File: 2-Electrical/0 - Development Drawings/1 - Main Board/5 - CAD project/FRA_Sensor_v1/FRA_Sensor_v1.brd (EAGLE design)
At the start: 79 x 94 mm, 141 parts, among them IC1 CP2101, IC2 LMV611, IC3 TS520533, J2 ETH_CONN, J3 USB, Q1 Si2300DS, Q2 FDN306P, T1 BC847, T2 BC847, T3 BC847, U2 ESP-WROOM-32, Y3 32.768kHz

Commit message: sch
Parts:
- removed C21, C22: 10u, resistor:C0603K
- removed C23: 220u, resistor:153CLV-0605
- removed C31: 100n, resistor:C0603K
- removed C8: DNI, resistor:C0603K
- removed L1: 2.2uH, resistor:L3225M
- removed LIGHT_DR: LDR, pinhead:1X02
- removed R20: 1G, resistor:R0603
- removed R26: 0, resistor:R0603
- removed R27: DNI, resistor:R0603
- removed R41, R45, R46: 12k, resistor:R0603
- removed TP13, TP28, TP29, TP30: TPTP10R, testpad:TP10R
- added D4, D6: PESD1CAN, diode:SOT23
- added D7, D8: (no value), SparkFun-LED:LED_5MM
- added J1: (no value), con-jack:SPC4078
- added LIGHT_DR1: LDR, pinhead:1X02
- added R68, R69: 10K, resistor:R0603
- added S1, S2: (no value), adafruit:B3F-31XX
- added TP1, TP2, TP3, TP4: TPTP10R, testpad:TP10R
- added U$5, U$6: MOUNTINGHOLE3.0THIN, microbuilder:MOUNTINGHOLE_3.0_PLATEDTHIN
- added X1: TB001-500-02BE, con-wago-500:W237-102
- C10, C17: value 10u -> DNI
- C29, C30: value 22p(DNI) -> 22p
- C7: value DNI -> 220u; device resistor:C0603K -> resistor:153CLV-0605
- R14: value 220k -> 100
- R15: value 100k -> 100
- R18: value 2M7 -> 100
- R19: value 47k -> 100
- R53, R54: value 10k -> 100k
- moved R14 611.4 mm to (-141.0, -533.4), turned to 0 degrees
- moved R15 601.1 mm to (-141.0, -538.5), flipped to the top, turned to 0 degrees
- moved R19 576.8 mm to (-141.0, -548.6), turned to 0 degrees
- moved R18 567.6 mm to (-141.0, -543.6), turned to 0 degrees
- moved C7 244.8 mm to (-119.4, -486.4)
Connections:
- net N$12 renamed P_RTC
- net N$13 renamed N_RTC
- removed net ADC: C31.2, R14.2, R15.2
- removed net N$14: LIGHT_DR.2, R14.1, R18.1, R19.2, R20.1
- removed net N$16: D3.1
- removed net N$27: R41.1
- removed net N$37: L1.1
- removed net N$40: R45.2, R46.1
- removed net N$9: C7.1, C8.2, R26.2, R27.1
- new net BTN1: R68.1, S1.1, U2.24
- new net BTN2: R69.1, S2.1, U2.26
- new net LED: R18.2, R19.2, U2.27
- new net N$6: D8.A, R18.1, R19.1
- new net N$7: D7.A, R14.1, R15.1
- net 3.3V: now also D6.3, R14.2, R15.2, R68.2, R69.2, TP2.TP; no longer C21.1, C23.+, C8.1, L1.2, LIGHT_DR.1, R18.2, R20.2, R26.1, R46.2, TP11.TP
- net 5V: now also TP3.TP; no longer C22.1, R41.2, TP28.TP, TP29.TP
- net GND: now also C7.-, D4.1, D4.2, D6.1, D6.2, D7.K, D8.K, J1.1, J1.2, S1.2, S2.2, X1.2; no longer C21.2, C22.2, C23.-, C31.1, C7.2, R15.1, R19.1, R27.2, R45.1, TP13.TP, TP30.TP
- net N$22: now also TP4.TP
- net N$23: now also TP1.TP
- net N$35: no longer C20.2
- net NRST: now also JTAG1.10, U$2.1
- net RXD0: now also U$2.5
- net TXD0: now also U$2.3
- net VIN: now also D4.3, J1.3, X1.1
- net VIN_PROTECTED: now also C7.+, TP11.TP
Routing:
- net GND: track 469.8 -> 80.2 mm, vias 29 -> 10
- net 3.3V: track 306.9 -> 29.1 mm, vias 26 -> 17
- net 5V: track 183.5 -> 5.38 mm, vias 9 -> 0
- net PWM: track 118.3 -> 0.00 mm, vias 3 -> 0
- net N$14: track 117.3 -> 0.00 mm, vias 2 -> 0
- net ADC: track 70.3 -> 0.00 mm, vias 5 -> 0
- net N$40: track 22.6 -> 0.00 mm, vias 2 -> 0
- net N$27: track 18.0 -> 0.00 mm, vias 2 -> 0
- net N$16: track 5.14 -> 0.00 mm
- net P_RTC: track 6.97 -> 2.57 mm
- net N_RTC: track 7.27 -> 3.60 mm
- net N$35: track 4.44 -> 2.12 mm
- net N$37: track 0.64 -> 0.00 mm
- removed copper zone on layer 1, net 5V
- removed copper zone on layer 16, net 5V
- removed copper zone on layer 16, net VBAT
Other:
- board text added: "06/2019"
- board text added: "FRA Sensor Unit Main PCB"
- board text removed: "12/2018"
- board text removed: "Alarm Light v2"
- board text removed: "X"
- board text removed: "Y"
- board text removed: "Z"

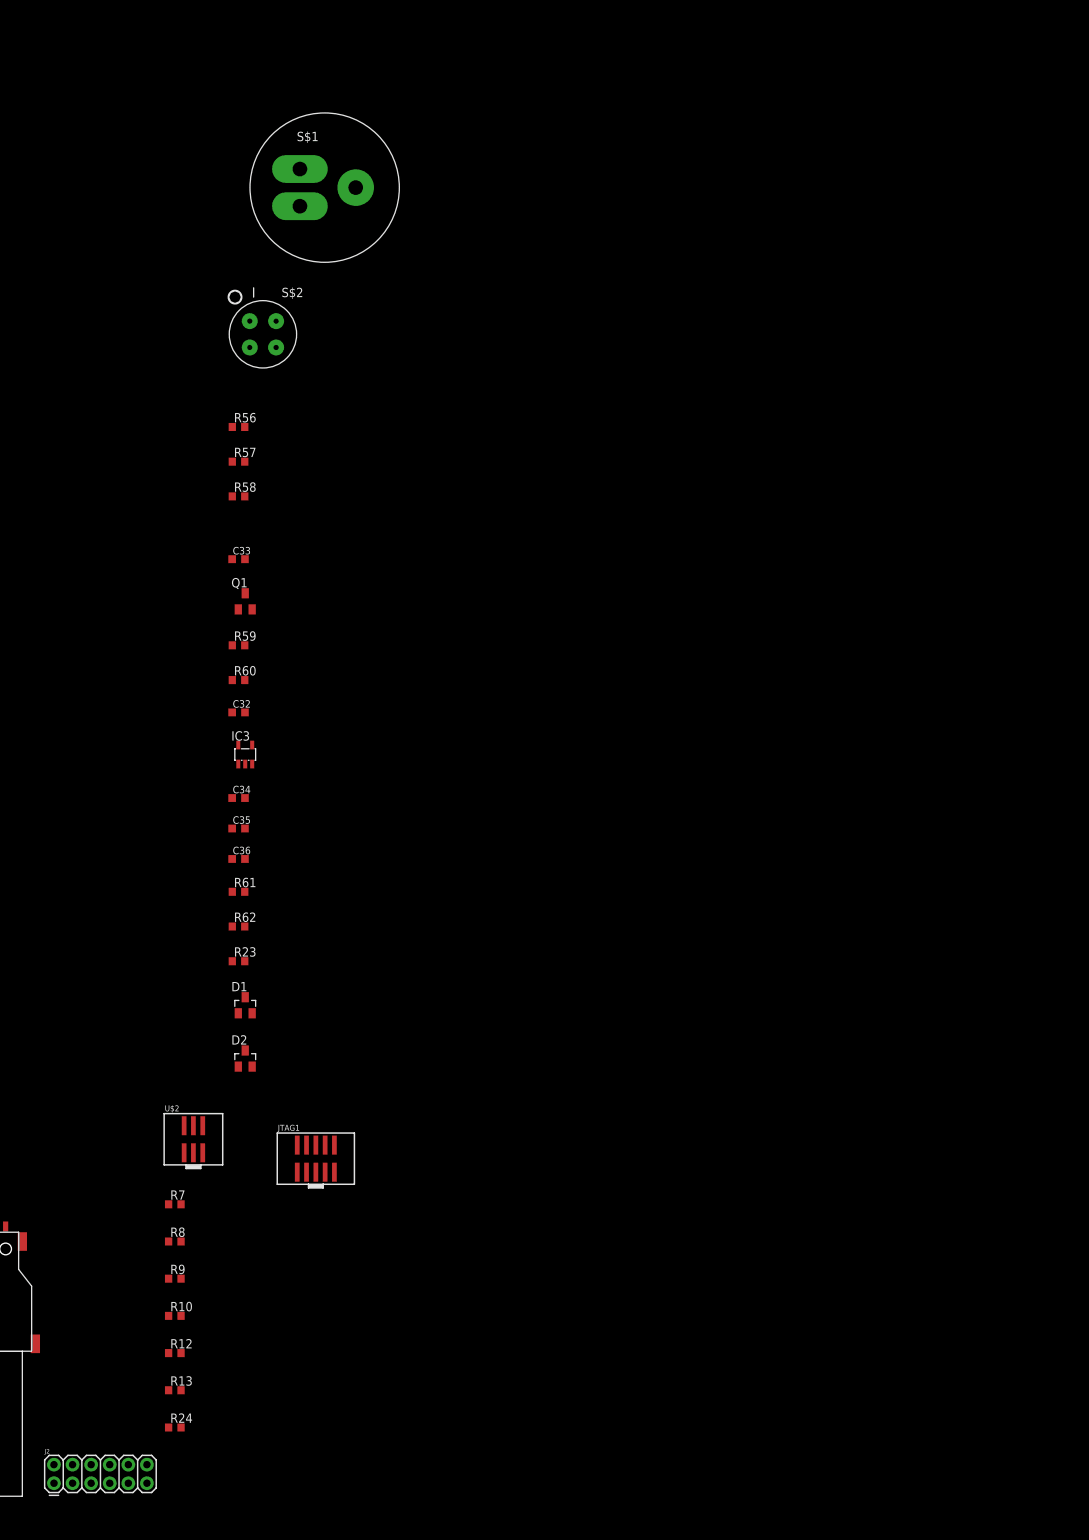
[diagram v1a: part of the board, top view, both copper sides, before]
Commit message: dev and sd
mac address changed
other sample testing
sd card example setup
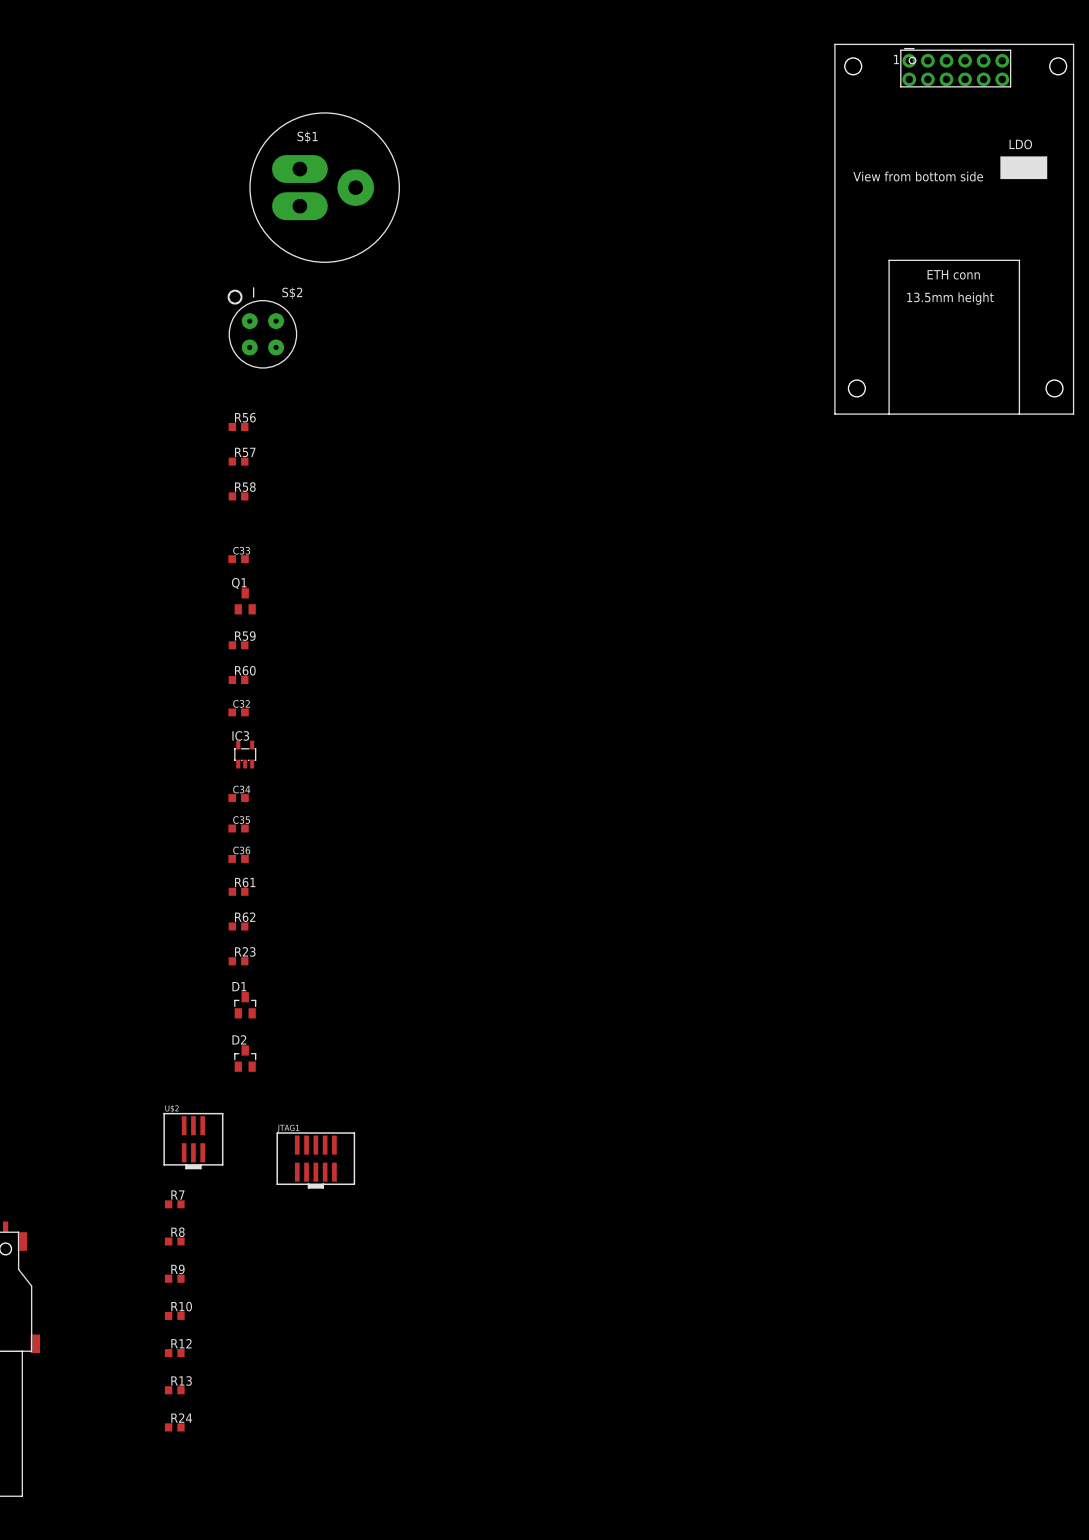
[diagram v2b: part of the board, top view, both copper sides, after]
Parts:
- added U$7: ETH_MODULE_OUTLINE, FRA_eagle_lib:ETH_MODULE_OUTLINE
- moved J2 226.7 mm to (73.7, -30.5), flipped to the bottom, turned to 180 degrees
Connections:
- new net ETH_5V: J2.12
- new net ETH_CLKOUT: J2.9
- new net ETH_INT: J2.10
- new net ETH_RST: J2.4
- new net ETH_WOL: J2.7
- net 3.3V: now also C39.1, C40.1, J2.2
- net BTN1: no longer U2.24
- net BTN2: no longer U2.26
- net GND: now also J2.1, J2.11
- net SD_CS_MCU: now also U2.28; no longer U2.10
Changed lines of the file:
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@@
 <element name="R24" library="resistor" package="R0603" value="100" x="-26.67" y="-217.17"/>
 <element name="U$3" library="adafruit" package="MICROSD" value="MICROSD" x="-67.31" y="-191.77"/>
-<element name="J2" library="SparkFun-Connectors" package="2X6" value="ETH_CONN" x="-43.18" y="-224.79">
-<attribute name="PROD_ID" value="CONN-12423" x="-43.18" y="-224.79" size="1.778" layer="27" display="off"/>
+<element name="J2" library="SparkFun-Connectors" package="2X6" value="ETH_CONN" x="73.66" y="-30.48" rot="MR180">
+<attribute name="PROD_ID" value="CONN-12423" x="73.66" y="-30.48" size="1.778" layer="28" rot="MR180" display="off"/>
 </element>
 <element name="J4" library="sd-mmc" package="SDCMF-10915W010" value="" x="-59.69" y="-203.2"/>
@@
 <element name="R18" library="resistor" package="R0603" value="100" x="-140.97" y="-543.56"/>
 <element name="R19" library="resistor" package="R0603" value="100" x="-140.97" y="-548.64"/>
+<element name="U$7" library="FRA_eagle_lib" package="ETH_MODULE_OUTLINE" value="ETH_MODULE_OUTLINE" x="63.5" y="-78.74"/>
 </elements>
 <signals>
@@
 <contactref element="S2" pad="2"/>
 <contactref element="S1" pad="2"/>
+<contactref element="J2" pad="1"/>
+<contactref element="J2" pad="11"/>
 <wire x1="-53.71" y1="-206.21" x2="-45.72" y2="-205.74" width="0" layer="19" extent="1-1"/>
 <wire x1="-63.81" y1="-202.81" x2="-53.71" y2="-206.21" width="0" layer="19" extent="1-1"/>
@@
 <wire x1="-72.898" y1="-191.77" x2="-65.024" y2="-189.738" width="0" layer="19" extent="1-1"/>
 <wire x1="-47.498" y1="-191.77" x2="-57.404" y2="-189.738" width="0" layer="19" extent="1-1"/>
+<wire x1="73.66" y1="-30.48" x2="-45.72" y2="-205.74" width="0" layer="19" extent="1-1"/>
+<wire x1="86.36" y1="-30.48" x2="73.66" y2="-30.48" width="0" layer="19" extent="1-1"/>
 <wire x1="-25.82" y1="-196.85" x2="-45.72" y2="-205.74" width="0" layer="19" extent="1-1"/>
 <wire x1="-24.13" y1="-175.95" x2="-25.82" y2="-196.85" width="0" layer="19" extent="1-1"/>
@@
 <wire x1="-18.816465625" y1="-89.983859375" x2="-17.088265625" y2="-98.564190625" width="0" layer="19" extent="1-1"/>
 <wire x1="-17.116465625" y1="-80.501196875" x2="-18.816465625" y2="-89.983859375" width="0" layer="19" extent="1-1"/>
-<wire x1="-72.07" y1="-257.84" x2="-72.898" y2="-205.74" width="0" layer="19" extent="1-1"/>
+<wire x1="-72.07" y1="-257.84" x2="73.66" y2="-30.48" width="0" layer="19" extent="1-1"/>
 <wire x1="-70.245" y1="-276.86" x2="-72.07" y2="-257.84" width="0" layer="19" extent="1-1"/>
 <wire x1="-70.245" y1="-281.94" x2="-70.245" y2="-276.86" width="0" layer="19" extent="1-1"/>
@@
 <wire x1="40.768428125" y1="4.974340625" x2="-17.116465625" y2="-80.501196875" width="0" layer="19" extent="1-1"/>
 <wire x1="44.7675" y1="3.595" x2="40.768428125" y2="4.974340625" width="0" layer="19" extent="1-1"/>
+<wire x1="48.9975" y1="3.4925" x2="44.7675" y2="3.595" width="0" layer="19" extent="1-1"/>
+<wire x1="56.4125" y1="6.985" x2="48.9975" y2="3.4925" width="0" layer="19" extent="1-1"/>
+<wire x1="52.3875" y1="11.43" x2="56.4125" y2="6.985" width="0" layer="19" extent="1-1"/>
+<wire x1="41.91" y1="25.64" x2="47.3075" y2="13.97" width="0" layer="19" extent="1-16"/>
+<wire x1="27.94" y1="34.29" x2="34.925" y2="25.64" width="0" layer="19" extent="16-16"/>
+<wire x1="29.5275" y1="36.195" x2="27.94" y2="34.29" width="0" layer="19" extent="1-1"/>
+<wire x1="13.6525" y1="34.5025" x2="27.94" y2="34.29" width="0" layer="19" extent="16-16"/>
+<wire x1="5.715" y1="54.37" x2="5.715" y2="54.2925" width="0" layer="19" extent="16-16"/>
+<wire x1="66.1175" y1="21.9075" x2="52.3875" y2="11.43" width="0" layer="19" extent="1-16"/>
+<wire x1="75.2475" y1="13.0175" x2="66.1175" y2="21.9075" width="0" layer="19" extent="16-16"/>
+<wire x1="69.5325" y1="46.355" x2="66.1175" y2="24.13" width="0" layer="19" extent="16-16"/>
+<wire x1="69.5325" y1="49.2125" x2="69.5325" y2="46.355" width="0" layer="19" extent="1-1"/>
+<wire x1="63.1825" y1="50.165" x2="69.5325" y2="49.2125" width="0" layer="19" extent="1-1"/>
+<wire x1="54.9275" y1="45.4025" x2="63.1825" y2="50.165" width="0" layer="19" extent="1-1"/>
+<wire x1="52.07" y1="55.245" x2="54.9275" y2="45.4025" width="0" layer="19" extent="1-1"/>
+<wire x1="77.2" y1="58.31" x2="69.5325" y2="49.2125" width="0" layer="19" extent="1-1"/>
+<wire x1="69.5" y1="67.31" x2="77.2" y2="58.31" width="0" layer="19" extent="1-1"/>
+<wire x1="77.2" y1="76.31" x2="70.135" y2="67.945" width="0" layer="19" extent="1-1"/>
+<wire x1="76.7575" y1="79.0575" x2="77.2" y2="76.31" width="0" layer="19" extent="1-1"/>
+<wire x1="68.58" y1="84.47" x2="76.7575" y2="81.915" width="0" layer="19" extent="1-1"/>
 </signal>
 <signal name="5V">
@@
 <contactref element="R14" pad="2"/>
 <contactref element="R15" pad="2"/>
+<contactref element="J2" pad="2"/>
+<contactref element="C39" pad="1"/>
+<contactref element="C40" pad="1"/>
 <wire x1="-70.27" y1="-427.99" x2="-70.27" y2="-433.07" width="0" layer="19" extent="1-1"/>
 <wire x1="-70.27" y1="-448.31" x2="-70.27" y2="-433.07" width="0" layer="19" extent="1-1"/>
-<wire x1="-90.59" y1="-463.55" x2="-70.27" y2="-448.31" width="0" layer="19" extent="1-1"/>
+<wire x1="-71.995" y1="-453.39" x2="-70.27" y2="-448.31" width="0" layer="19" extent="1-1"/>
+<wire x1="-71.995" y1="-458.47" x2="-71.995" y2="-453.39" width="0" layer="19" extent="1-1"/>
+<wire x1="-90.59" y1="-463.55" x2="-71.995" y2="-458.47" width="0" layer="19" extent="1-1"/>
 <wire x1="-90.59" y1="-468.63" x2="-90.59" y2="-463.55" width="0" layer="19" extent="1-1"/>
 <wire x1="-121.92" y1="-499.11" x2="-90.59" y2="-468.63" width="0" layer="19" extent="1-1"/>
@@
 <wire x1="-71.995" y1="-292.1" x2="-71.995" y2="-297.18" width="0" layer="19" extent="1-1"/>
 <wire x1="-71.995" y1="-287.02" x2="-71.995" y2="-292.1" width="0" layer="19" extent="1-1"/>
-<wire x1="-25.82" y1="-191.77" x2="-71.995" y2="-287.02" width="0" layer="19" extent="1-1"/>
+<wire x1="73.66" y1="-33.02" x2="-71.995" y2="-287.02" width="0" layer="19" extent="1-1"/>
+<wire x1="-25.82" y1="-191.77" x2="73.66" y2="-33.02" width="0" layer="19" extent="1-1"/>
 <wire x1="-27.52" y1="-186.69" x2="-25.82" y2="-191.77" width="0" layer="19" extent="1-1"/>
 <wire x1="-18.816465625" y1="-153.483171875" x2="-27.52" y2="-186.69" width="0" layer="19" extent="1-1"/>
 <wire x1="46.355" y1="9.8425" x2="-18.816465625" y2="-153.483171875" width="0" layer="19" extent="1-1"/>
 <wire x1="24.13" y1="54.2925" x2="34.925" y2="23.89" width="0" layer="19" extent="16-16"/>
+<wire x1="20.955" y1="54.2925" x2="24.13" y2="54.2925" width="0" layer="19" extent="1-1"/>
+<wire x1="20.955" y1="56.515" x2="20.955" y2="54.2925" width="0" layer="19" extent="1-1"/>
 <wire x1="23.495" y1="66.675" x2="20.955" y2="56.515" width="0" layer="19" extent="1-1"/>
 <wire x1="25.0825" y1="66.675" x2="23.495" y2="66.675" width="0" layer="19" extent="1-1"/>
@@
 <wire x1="-70.27" y1="-422.91" x2="-59.41" y2="-202.01" width="0" layer="19" extent="1-1"/>
 </signal>
-<signal name="SD_CS_MCU">
-<contactref element="U2" pad="10"/>
-<contactref element="R63" pad="1"/>
-<wire x1="65.77" y1="76.31" x2="-71.97" y2="-422.91" width="0" layer="19" extent="1-1"/>
-</signal>
 <signal name="ETH_CS">
 <contactref element="R48" pad="2"/>
@@
 </signal>
 <signal name="BTN1">
-<contactref element="U2" pad="24"/>
 <contactref element="R68" pad="1"/>
 <contactref element="S1" pad="1"/>
-<wire x1="-81.0006" y1="-454.6346" x2="59.2" y2="61.595" width="0" layer="19" extent="1-1"/>
-<wire x1="-92.29" y1="-463.55" x2="-81.0006" y2="-454.6346" width="0" layer="19" extent="1-1"/>
+<wire x1="-81.0006" y1="-454.6346" x2="-92.29" y2="-463.55" width="0" layer="19" extent="1-1"/>
 </signal>
 <signal name="BTN2">
-<contactref element="U2" pad="26"/>
 <contactref element="R69" pad="1"/>
 <contactref element="S2" pad="1"/>
-<wire x1="-91.1606" y1="-454.6346" x2="61.96" y2="58.31" width="0" layer="19" extent="1-1"/>
-<wire x1="-92.29" y1="-468.63" x2="-91.1606" y2="-454.6346" width="0" layer="19" extent="1-1"/>
+<wire x1="-91.1606" y1="-454.6346" x2="-92.29" y2="-468.63" width="0" layer="19" extent="1-1"/>
 </signal>
 <signal name="N$7">
@@
 <wire x1="-140.97" y1="-525.78" x2="-141.82" y2="-543.56" width="0" layer="19" extent="1-1"/>
 </signal>
+<signal name="ETH_RST">
+<contactref element="J2" pad="4"/>
+</signal>
+<signal name="ETH_5V">
+<contactref element="J2" pad="12"/>
+</signal>
+<signal name="ETH_INT">
+<contactref element="J2" pad="10"/>
+</signal>
+<signal name="ETH_CLKOUT">
+<contactref element="J2" pad="9"/>
+</signal>
+<signal name="ETH_WOL">
+<contactref element="J2" pad="7"/>
+</signal>
+<signal name="SD_CS_MCU">
+<contactref element="R63" pad="1"/>
+<contactref element="U2" pad="28"/>
+<wire x1="64.5" y1="58.31" x2="-71.97" y2="-422.91" width="0" layer="19" extent="1-1"/>
+</signal>
 </signals>

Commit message: placment drafts
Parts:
- removed LED_12: LED_ring_12, pinhead:1X04
- added SENSOR_1, SENSOR_10, SENSOR_2, SENSOR_3, SENSOR_4, SENSOR_5, SENSOR_6, SENSOR_7, SENSOR_8, SENSOR_9: SENS1, pinhead:1X04
- moved D7 597.4 mm to (94.0, 26.7), turned to 90 degrees
- moved D8 590.5 mm to (94.0, 16.5), turned to 90 degrees
- moved S1 563.9 mm to (96.5, 82.5), turned to 90 degrees
- moved X1 555.4 mm to (94.0, 54.6), turned to 90 degrees
- moved S2 553.9 mm to (96.5, 68.6), turned to 90 degrees
- moved J1 552.5 mm to (88.9, 39.4), turned to 180 degrees
- moved U$3 224.8 mm to (20.3, 15.2)
- moved J4 224.8 mm to (27.9, 3.81)
- moved C2 204.9 mm to (239.4, 37.5)
- moved IC1 204.9 mm to (256.9, 24.1)
- moved R2 204.9 mm to (268.3, 15.6)
- moved R21 204.9 mm to (249.2, 17.1)
- moved R25 204.9 mm to (281.3, 55.2)
- moved R39 204.9 mm to (213.4, 49.2)
- moved R40 204.9 mm to (260.0, 19.7)
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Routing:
- net RXD0: track 117.5 -> 0.00 mm, vias 6 -> 0
- net TXD0: track 111.6 -> 0.00 mm, vias 7 -> 0
- net GND: track 80.2 -> 26.3 mm, vias 10 -> 7
- net NRST: track 36.5 -> 0.00 mm, vias 2 -> 0
- net N$36: track 26.8 -> 4.70 mm
- net SHIELD: track 25.0 -> 3.24 mm
- net 5V: track 5.38 -> 2.22 mm
- net N$26: track 3.79 -> 0.87 mm
- net D_P: track 7.53 -> 4.76 mm
- net D_N: track 6.62 -> 4.06 mm
- net 3.3V: vias 17 -> 3
- removed copper zone on layer 1, net 3.3V
- removed copper zone on layer 16, net 3.3V
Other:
- board size 79 x 94 mm -> 100 x 100 mm
